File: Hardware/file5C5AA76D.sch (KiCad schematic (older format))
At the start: 12 parts, among them J14 Conn_01x04_Female, J29 SID_Audio_Connector, U5 MAX7375AXR105, U6 74HC595, U7 74HC595, U8 SID

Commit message: IT WORKS
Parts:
- removed C38: 2200 uF, Capacitor_SMD:CP_Elec_10x10, symbol Device:CP
- added C38, C50: 1 uF, Capacitor_SMD:C_0603_1608Metric, symbol Device:C
- added C47, C48, C49: 100 nF, Capacitor_SMD:C_0603_1608Metric, symbol Device:C
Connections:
- net +5V: now also C38.1, C47.2, C48.1, C49.2, C50.1
- net GND: now also C38.2, C47.1, C48.2, C49.1, C50.2
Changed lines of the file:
@@
 	6550 3450 6650 3450
 Wire Wire Line
-	4850 2950 4850 3200
+	4850 2950 4850 3100
 $Comp
 L power:+5V #PWR?
@@
 	3250 4450 3250 3900
 Wire Wire Line
-	3250 3900 4400 3900
+	3250 3900 3400 3900
 Connection ~ 3800 4450
 Connection ~ 4400 3900
@@
 $EndComp
 Wire Wire Line
-	9200 2900 9200 2750
+	9200 2900 9200 2850
 Connection ~ 9200 2450
 Wire Wire Line
 	9200 1500 9200 2450
-$Comp
-L Device:CP C38
-U 1 1 5BDEB869
-P 9700 2600
-F 0 "C38" H 9818 2646 50  0000 L CNN
-F 1 "2200 uF" H 9818 2555 50  0000 L CNN
-F 2 "Capacitor_SMD:CP_Elec_10x10" H 9738 2450 50  0001 C CNN
-F 3 "~" H 9700 2600 50  0001 C CNN
-	1    9700 2600
-	1    0    0    -1
-$EndComp
-$Comp
-L power:GND #PWR?
-U 1 1 5BDEB8C2
-P 9700 2900
-AR Path="/5BDEB8C2" Ref="#PWR?"  Part="1"
-AR Path="/5C5AA76E/5BDEB8C2" Ref="#PWR0116"  Part="1"
-F 0 "#PWR0116" H 9700 2650 50  0001 C CNN
-F 1 "GND" H 9705 2727 50  0000 C CNN
-F 2 "" H 9700 2900 50  0001 C CNN
-F 3 "" H 9700 2900 50  0001 C CNN
-	1    9700 2900
-	1    0    0    -1
-$EndComp
-Wire Wire Line
-	9700 2900 9700 2750
-Wire Wire Line
-	9700 2450 9200 2450
 Wire Wire Line
 	5250 2650 6650 2650
@@
 $EndComp
 Wire Wire Line
-	4850 2200 4850 2350
+	4850 2200 4850 2300
+$Comp
+L Device:C C48
+U 1 1 5C86A2C9
+P 3750 2700
+F 0 "C48" H 3865 2746 50  0000 L CNN
+F 1 "100 nF" H 3865 2655 50  0000 L CNN
+F 2 "Capacitor_SMD:C_0603_1608Metric" H 3788 2550 50  0001 C CNN
+F 3 "~" H 3750 2700 50  0001 C CNN
+	1    3750 2700
+	1    0    0    -1
+$EndComp
+$Comp
+L Device:C C38
+U 1 1 5C86A314
+P 3350 2700
+F 0 "C38" H 3465 2746 50  0000 L CNN
+F 1 "1 uF" H 3465 2655 50  0000 L CNN
+F 2 "Capacitor_SMD:C_0603_1608Metric" H 3388 2550 50  0001 C CNN
+F 3 "~" H 3350 2700 50  0001 C CNN
+	1    3350 2700
+	1    0    0    -1
+$EndComp
+Wire Wire Line
+	3350 2850 3350 3100
+Wire Wire Line
+	3350 3100 3750 3100
+Connection ~ 4850 3100
+Wire Wire Line
+	4850 3100 4850 3200
+Wire Wire Line
+	3750 2850 3750 3100
+Connection ~ 3750 3100
+Wire Wire Line
+	3750 3100 4850 3100
+Wire Wire Line
+	3750 2550 3750 2300
+Wire Wire Line
+	3750 2300 4850 2300
+Connection ~ 4850 2300
+Wire Wire Line
+	4850 2300 4850 2350
+Wire Wire Line
+	3350 2550 3350 2300
+Wire Wire Line
+	3350 2300 3750 2300
+Connection ~ 3750 2300
+$Comp
+L Device:C C50
+U 1 1 5C88C596
+P 9700 2600
+F 0 "C50" H 9815 2646 50  0000 L CNN
+F 1 "1 uF" H 9815 2555 50  0000 L CNN
+F 2 "Capacitor_SMD:C_0603_1608Metric" H 9738 2450 50  0001 C CNN
+F 3 "~" H 9700 2600 50  0001 C CNN
+	1    9700 2600
+	1    0    0    -1
+$EndComp
+Wire Wire Line
+	9700 2750 9700 2850
+Wire Wire Line
+	9700 2850 9200 2850
+Connection ~ 9200 2850
+Wire Wire Line
+	9200 2850 9200 2750
+Wire Wire Line
+	9700 2450 9200 2450
+$Comp
+L Device:C C49
+U 1 1 5C8935D6
+P 4000 3750
+F 0 "C49" H 4115 3796 50  0000 L CNN
+F 1 "100 nF" H 4115 3705 50  0000 L CNN
+F 2 "Capacitor_SMD:C_0603_1608Metric" H 4038 3600 50  0001 C CNN
+F 3 "~" H 4000 3750 50  0001 C CNN
+	1    4000 3750
+	1    0    0    -1
+$EndComp
+Connection ~ 4000 3900
+Wire Wire Line
+	4000 3900 4400 3900
+$Comp
+L Device:C C47
+U 1 1 5C89361B
+P 3400 3750
+F 0 "C47" H 3515 3796 50  0000 L CNN
+F 1 "100 nF" H 3515 3705 50  0000 L CNN
+F 2 "Capacitor_SMD:C_0603_1608Metric" H 3438 3600 50  0001 C CNN
+F 3 "~" H 3400 3750 50  0001 C CNN
+	1    3400 3750
+	1    0    0    -1
+$EndComp
+Connection ~ 3400 3900
+Wire Wire Line
+	3400 3900 4000 3900
+$Comp
+L power:GND #PWR?
+U 1 1 5C893684
+P 3400 3550
+AR Path="/5C893684" Ref="#PWR?"  Part="1"
+AR Path="/5C5AA76E/5C893684" Ref="#PWR0116"  Part="1"
+F 0 "#PWR0116" H 3400 3300 50  0001 C CNN
+F 1 "GND" H 3405 3377 50  0000 C CNN
+F 2 "" H 3400 3550 50  0001 C CNN
+F 3 "" H 3400 3550 50  0001 C CNN
+	1    3400 3550
+	-1   0    0    1
+$EndComp
+$Comp
+L power:GND #PWR?
+U 1 1 5C8936CF
+P 4000 3550
+AR Path="/5C8936CF" Ref="#PWR?"  Part="1"
+AR Path="/5C5AA76E/5C8936CF" Ref="#PWR0121"  Part="1"
+F 0 "#PWR0121" H 4000 3300 50  0001 C CNN
+F 1 "GND" H 4005 3377 50  0000 C CNN
+F 2 "" H 4000 3550 50  0001 C CNN
+F 3 "" H 4000 3550 50  0001 C CNN
+	1    4000 3550
+	-1   0    0    1
+$EndComp
+Wire Wire Line
+	3400 3550 3400 3600
+Wire Wire Line
+	4000 3550 4000 3600
 Wire Bus Line
 	6200 3050 6200 4050

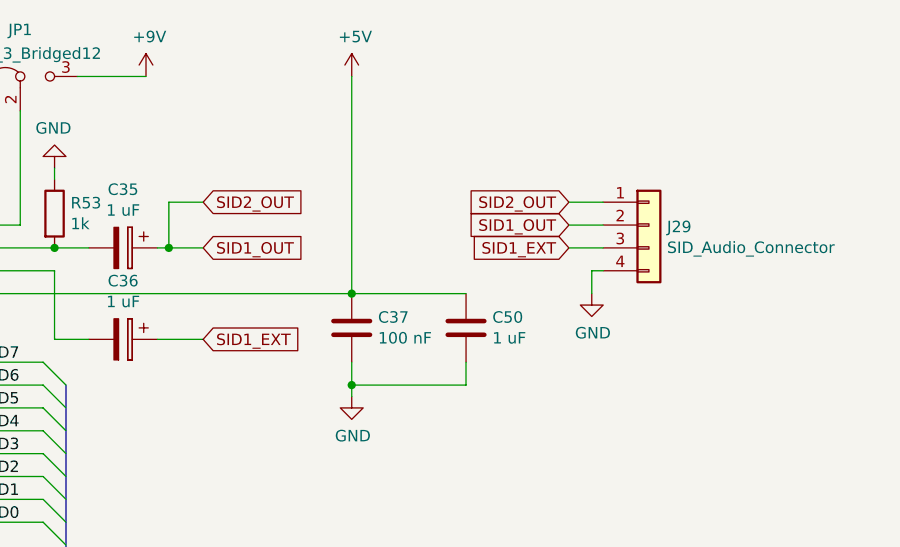
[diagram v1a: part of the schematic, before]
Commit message: Updated to single four layer board
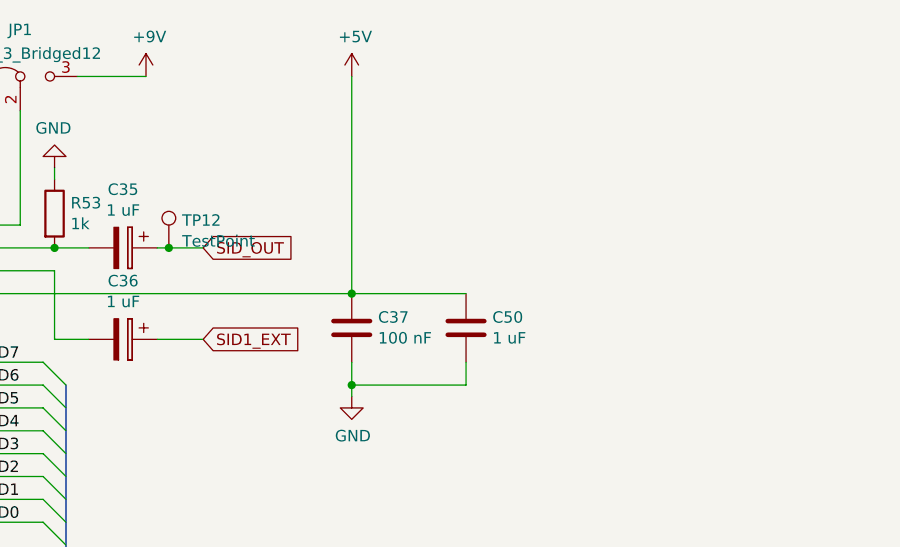
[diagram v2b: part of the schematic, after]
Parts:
- removed J29: SID_Audio_Connector, Connector_PinHeader_2.54mm:PinHeader_1x04_P2.54mm_Vertical, symbol Connector_Generic:Conn_01x04
- added TP12: TestPoint, TestPoint:TestPoint_Pad_D1.0mm, symbol Connector:TestPoint
- J14: footprint Connector_PinHeader_2.54mm:PinHeader_1x04_P2.54mm_Vertical -> Connector_PinSocket_2.54mm:PinSocket_1x04_P2.54mm_Vertical
- JP1: footprint Connector_PinHeader_2.54mm:PinHeader_1x03_P2.54mm_Vertical -> Connector_PinHeader_2.54mm:PinHeader_1x03_P2.54mm_Vertical_SMD_Pin1Left
- U8: footprint Package_DIP:DIP-28_W15.24mm_Socket -> Package_DIP:DIP-28_W16.51mm_SMDSocket_LongPads
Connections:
- net SID1_OUT renamed SID_OUT
- net SID_OUT: now also TP12.1
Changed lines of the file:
@@
 F 0 "U8" H 7075 3575 50  0000 C CNN
 F 1 "SID" H 7075 3484 50  0000 C CNN
-F 2 "Package_DIP:DIP-28_W15.24mm_Socket" H 6850 3300 50  0001 C CNN
+F 2 "Package_DIP:DIP-28_W16.51mm_SMDSocket_LongPads" H 6850 3300 50  0001 C CNN
 F 3 "" H 6850 3300 50  0001 C CNN
 	1    7100 2750
@@
 F 0 "JP1" H 7750 1704 50  0000 C CNN
 F 1 "Jumper_3_Bridged12" H 7750 1600 50  0000 C CNN
-F 2 "Connector_PinHeader_2.54mm:PinHeader_1x03_P2.54mm_Vertical" H 7750 1500 50  0001 C CNN
+F 2 "Connector_PinHeader_2.54mm:PinHeader_1x03_P2.54mm_Vertical_SMD_Pin1Left" H 7750 1500 50  0001 C CNN
 F 3 "~" H 7750 1500 50  0001 C CNN
 	1    7750 1500
@@
 F 0 "J14" H 6344 1925 50  0000 C CNN
 F 1 "Conn_01x04_Female" H 6344 2016 50  0000 C CNN
-F 2 "Connector_PinHeader_2.54mm:PinHeader_1x04_P2.54mm_Vertical" H 6450 2350 50  0001 C CNN
+F 2 "Connector_PinSocket_2.54mm:PinSocket_1x04_P2.54mm_Vertical" H 6450 2350 50  0001 C CNN
 F 3 "~" H 6450 2350 50  0001 C CNN
 	1    6450 2350
@@
 $EndComp
 Text GLabel 8550 2250 2    50   Input ~ 0
-SID1_OUT
+SID_OUT
 Connection ~ 7900 2250
 Wire Wire Line
@@
 $EndComp
 Wire Wire Line
-	8350 2250 8400 2250
-Wire Wire Line
 	8350 2650 8550 2650
-Text GLabel 8550 2050 2    50   Input ~ 0
-SID2_OUT
-Wire Wire Line
-	8550 2050 8400 2050
-Wire Wire Line
-	8400 2050 8400 2250
-Connection ~ 8400 2250
-Wire Wire Line
-	8400 2250 8550 2250
 $Comp
 L Device:CP C35
@@
 NoConn ~ 7500 2550
 NoConn ~ 7500 2650
-$Comp
-L Connector_Generic:Conn_01x04 J29
-U 1 1 5C596EAE
-P 10500 2150
-F 0 "J29" H 10579 2142 50  0000 L CNN
-F 1 "SID_Audio_Connector" H 10579 2051 50  0000 L CNN
-F 2 "Connector_PinHeader_2.54mm:PinHeader_1x04_P2.54mm_Vertical" H 10500 2150 50  0001 C CNN
-F 3 "~" H 10500 2150 50  0001 C CNN
-	1    10500 2150
-	1    0    0    -1
-$EndComp
-Text GLabel 10150 2050 0    50   Input ~ 0
-SID2_OUT
-Text GLabel 10150 2150 0    50   Input ~ 0
-SID1_OUT
-Text GLabel 10150 2250 0    50   Input ~ 0
-SID1_EXT
-$Comp
-L power:GND #PWR?
-U 1 1 5C59702B
-P 10250 2450
-AR Path="/5C59702B" Ref="#PWR?"  Part="1"
-AR Path="/5C5AA76E/5C59702B" Ref="#PWR027"  Part="1"
-F 0 "#PWR027" H 10250 2200 50  0001 C CNN
-F 1 "GND" H 10255 2277 50  0000 C CNN
-F 2 "" H 10250 2450 50  0001 C CNN
-F 3 "" H 10250 2450 50  0001 C CNN
-	1    10250 2450
-	1    0    0    -1
-$EndComp
-Wire Wire Line
-	10250 2450 10250 2350
-Wire Wire Line
-	10250 2350 10300 2350
-Wire Wire Line
-	10150 2250 10300 2250
-Wire Wire Line
-	10150 2150 10300 2150
-Wire Wire Line
-	10150 2050 10300 2050
 $Comp
 L Oscillator:MAX7375AXR105 U5
@@
 Wire Bus Line
 	6200 4050 6200 5400
+Wire Wire Line
+	8350 2250 8400 2250
+$Comp
+L Connector:TestPoint TP12
+U 1 1 5CBB3BCE
+P 8400 2250
+F 0 "TP12" H 8458 2370 50  0000 L CNN
+F 1 "TestPoint" H 8458 2279 50  0000 L CNN
+F 2 "TestPoint:TestPoint_Pad_D1.0mm" H 8600 2250 50  0001 C CNN
+F 3 "~" H 8600 2250 50  0001 C CNN
+	1    8400 2250
+	1    0    0    -1
+$EndComp
+Connection ~ 8400 2250
+Wire Wire Line
+	8400 2250 8550 2250
 $EndSCHEMATC
